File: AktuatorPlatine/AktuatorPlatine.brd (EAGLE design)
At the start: 31.7 x 56.2 mm, 12 parts, among them CON1 XT30UPB-M, IC1 L293D, IC2 L293D

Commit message: Platinen stuff vom Prototype ätzen
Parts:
- moved JP4 2.25 mm to (6.07, 42.2)
- moved JP3 1.49 mm to (6.07, 37.7)
- moved JP1 0.60 mm to (6.14, 28.0)
- moved JP2 0.21 mm to (6.14, 32.4)
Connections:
- net N$13: now also JP1.1, JP2.1, JP3.1, JP4.1; no longer JP1.2, JP2.2, JP3.2, JP4.2
- net N$15: now also JP4.2; no longer JP4.1
- net N$24: now also JP3.2; no longer JP3.1
- net N$25: now also JP2.2; no longer JP2.1
- net N$26: now also JP1.2; no longer JP1.1
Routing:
- net N$32: track 0.00 -> 174.9 mm
- net N$15: track 3.09 -> 8.02 mm
- net N$24: track 2.88 -> 7.69 mm
- net N$25: track 3.10 -> 7.86 mm
- net N$14: track 92.1 -> 96.6 mm
- net N$26: track 3.78 -> 7.51 mm
- net N$13: track 71.3 -> 73.5 mm
- net GND: track 103.7 -> 105.6 mm

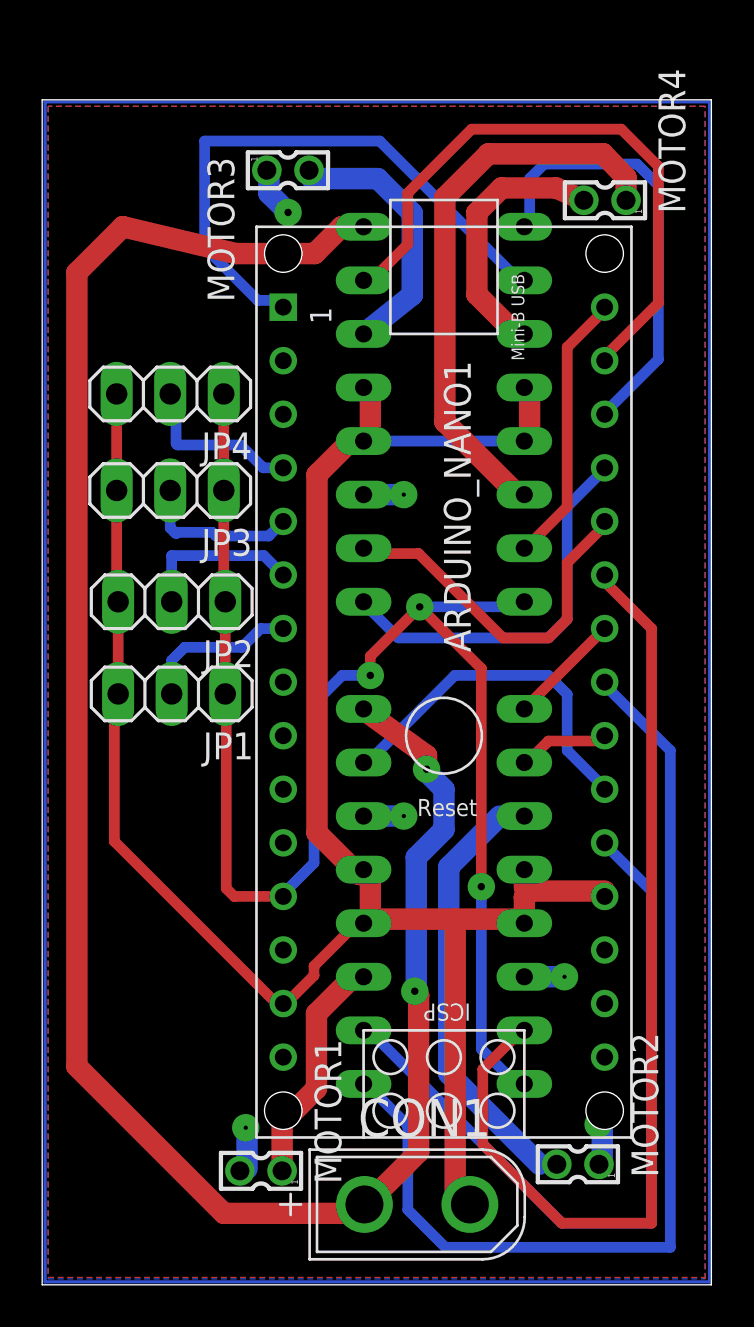
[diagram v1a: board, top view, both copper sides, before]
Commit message: More clearance
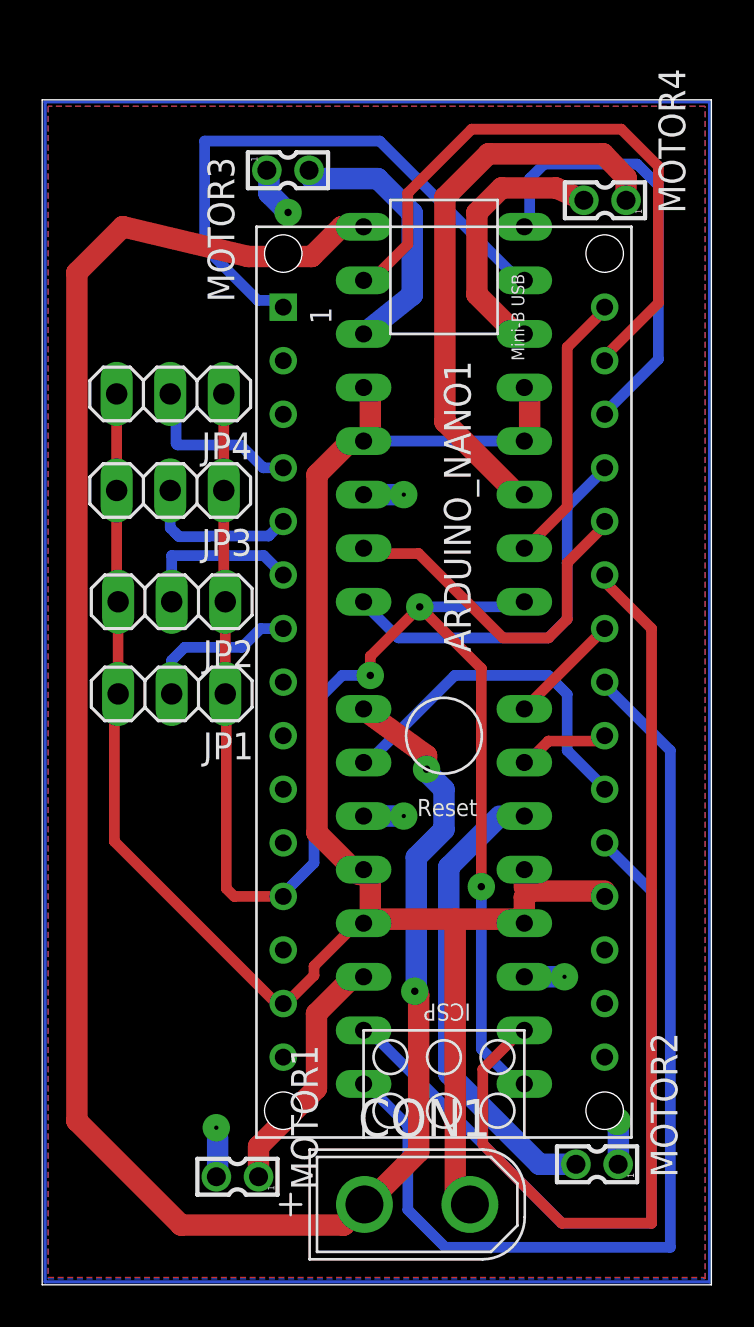
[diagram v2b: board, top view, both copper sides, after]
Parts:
- moved MOTOR1 1.15 mm to (9.26, 5.12)
- moved MOTOR2 0.91 mm to (26.3, 5.71)
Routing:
- net N$14: track 96.6 -> 98.6 mm
- net N$22: track 21.3 -> 22.2 mm
- net N$16: track 11.1 -> 11.8 mm
- net N$17: track 21.9 -> 22.7 mm
